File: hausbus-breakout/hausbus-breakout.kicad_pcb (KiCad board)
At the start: 2 copper layers, 29.2 x 32.5 mm, 17 parts, among them IC1 ATMEGA328P-M, P1 CONN_01X10, P2 CONN_01X10, P3 CONN_01X02, P4 CONN_01X02, U1 MCP2515-I/ST, U2 PCA82C251, Y1 16MHz

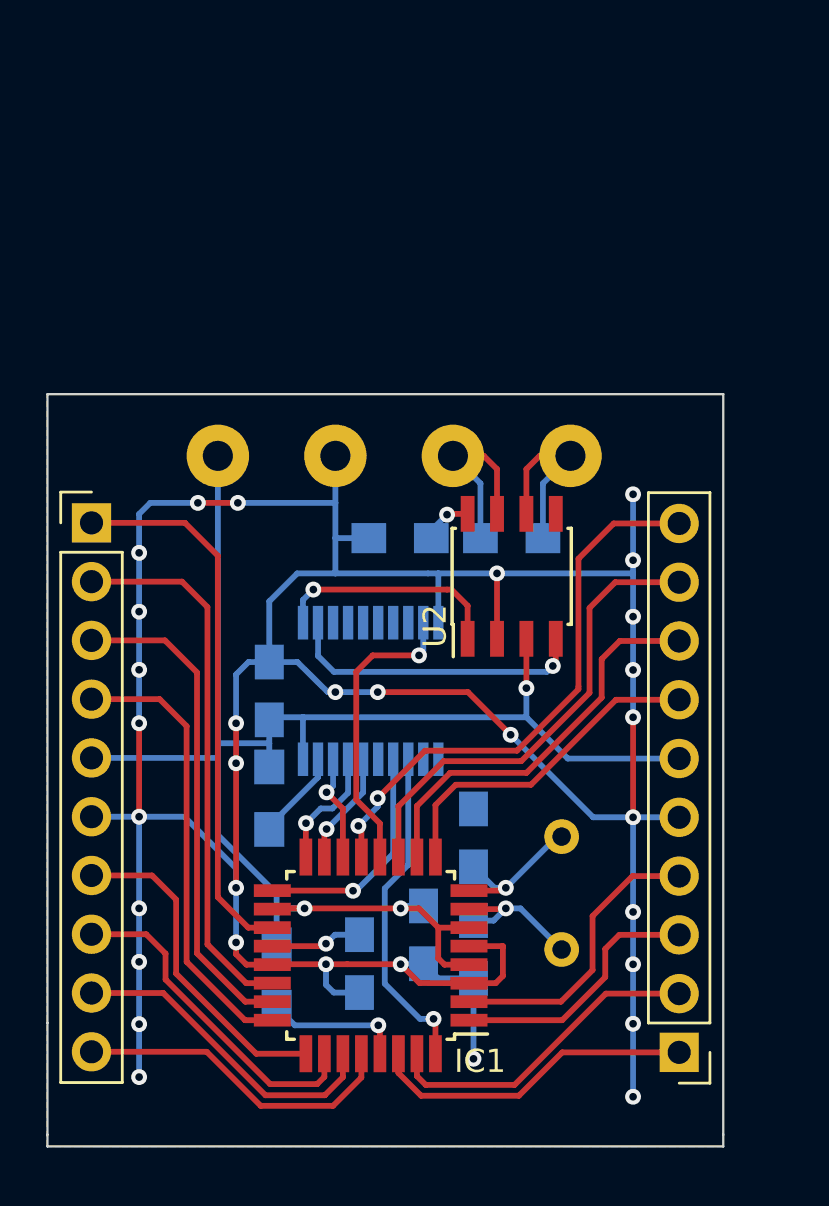
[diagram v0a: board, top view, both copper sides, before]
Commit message: updated breakout to have all four hardware pwm pins of timer 0 and 1 available
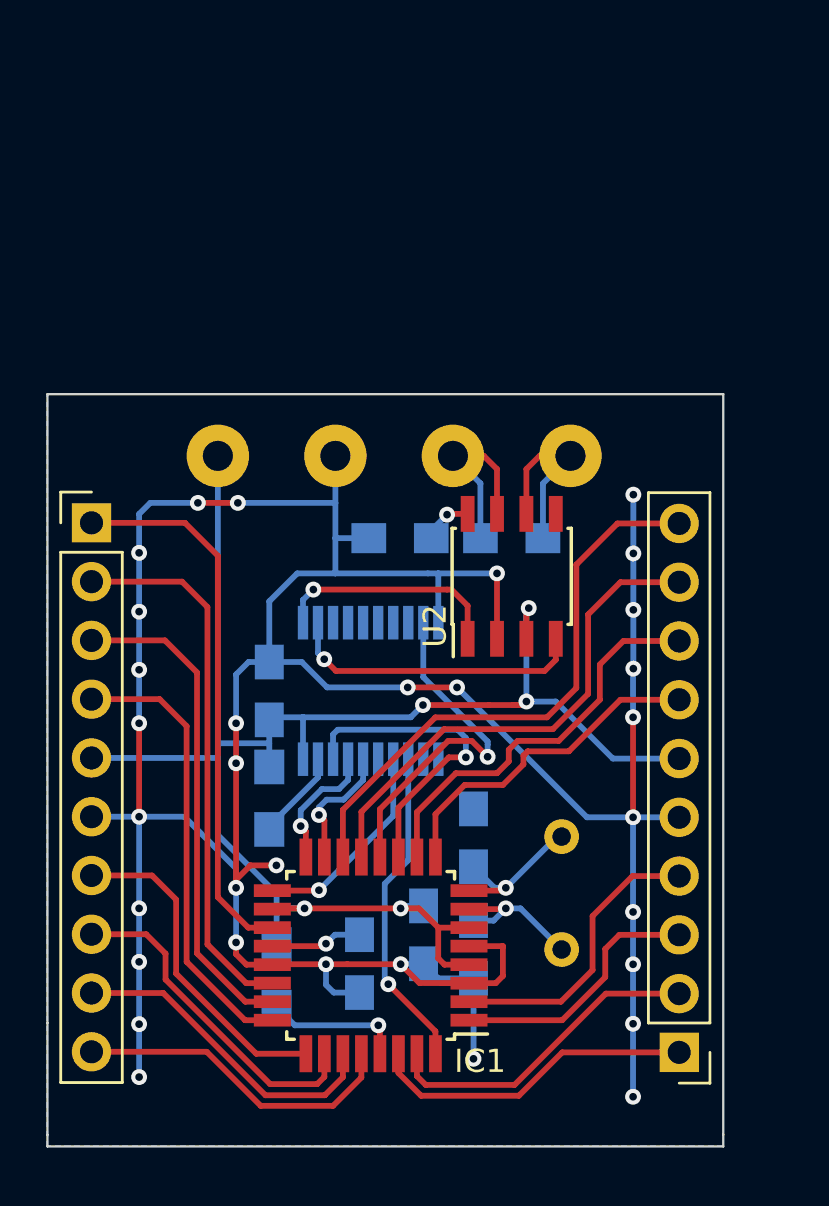
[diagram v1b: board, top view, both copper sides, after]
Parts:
- R1: value term. opt. -> 120R
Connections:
- IC1 pad 11: Net-(IC1-Pad11) -> SS
- IC1 pad 14: SS -> Net-(IC1-Pad14)
- P1 pad 10: Net-(IC1-Pad13) -> Net-(IC1-Pad14)
- P1 pad 9: Net-(IC1-Pad11) -> Net-(IC1-Pad13)
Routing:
- net Net-(IC1-Pad14): track 0.00 -> 24.8 mm
- net Net-(IC1-Pad11): track 20.5 -> 0.00 mm
- net SS: track 4.64 -> 13.8 mm
- net GND: track 156.0 -> 152.5 mm
- net +5V: track 69.8 -> 72.4 mm, vias 3 -> 5
- net Net-(IC1-Pad13): track 24.2 -> 21.8 mm, vias 2 -> 0
- net CLKO: track 12.9 -> 15.2 mm
- net SCK: track 9.97 -> 9.01 mm
- net MOSI: track 4.92 -> 5.55 mm
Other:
- board text added: "B2 B1 D6 D5 5V GND D4 D3 D1 D0"
- board text removed: "B1 D7 D6 D5 5V GND D4 D3 D1 D0"

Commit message: added usb2serial converter header
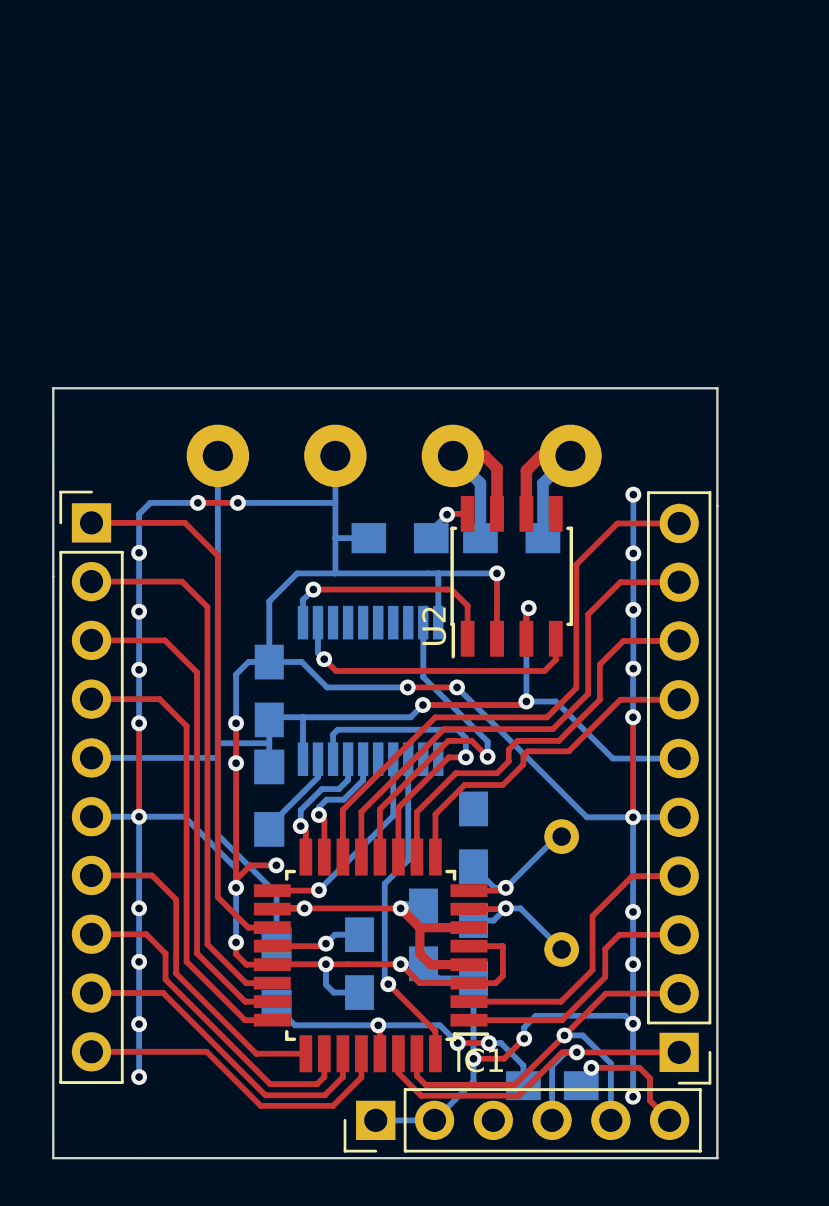
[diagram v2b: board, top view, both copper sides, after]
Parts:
- added C6: 100n, Capacitors_SMD:C_0805_HandSoldering, B.Cu at (215.6, 123.9)
- added P5: CONN_01X06, Socket_Strips:Socket_Strip_Straight_1x06_Pitch2.54mm, F.Cu at (208.0, 125.4)
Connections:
- net Net-(IC1-Pad29) renamed RS
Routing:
- net GND: track 152.5 -> 166.5 mm, vias 32 -> 33
- net RS: track 6.07 -> 13.9 mm, vias 1 -> 3
- net Net-(C6-Pad1): track 0.00 -> 5.85 mm, vias 0 -> 1
- net Net-(IC1-Pad31): track 14.1 -> 19.1 mm, vias 0 -> 1
- net Net-(IC1-Pad30): track 14.2 -> 17.8 mm, vias 0 -> 1
- net +5V: track 72.4 -> 73.1 mm
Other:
- board size 29.2 x 32.5 mm -> 28.7 x 33.3 mm
- net class buslines added: clearance 0.2, trace_width 0.5, via_dia 0.6858, via_drill 0.3302
- net class power added: clearance 0.2, trace_width 0.4, via_dia 0.6858, via_drill 0.3302
- board text added: "*B2 *B1 *D6 *D5 5V GND D4 D3 D1 D0"
- board text added: "ADC6 ADC7 C0 C1 5V GND C2 C3 C4 C5"
- board text removed: "B2 B1 D6 D5 5V GND D4 D3 D1 D0"
- board text removed: "C6 C7 C0 C1 5V GND C2 C3 C4 C5"

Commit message: cleanup of schematic, added rj45 jacks for can bus
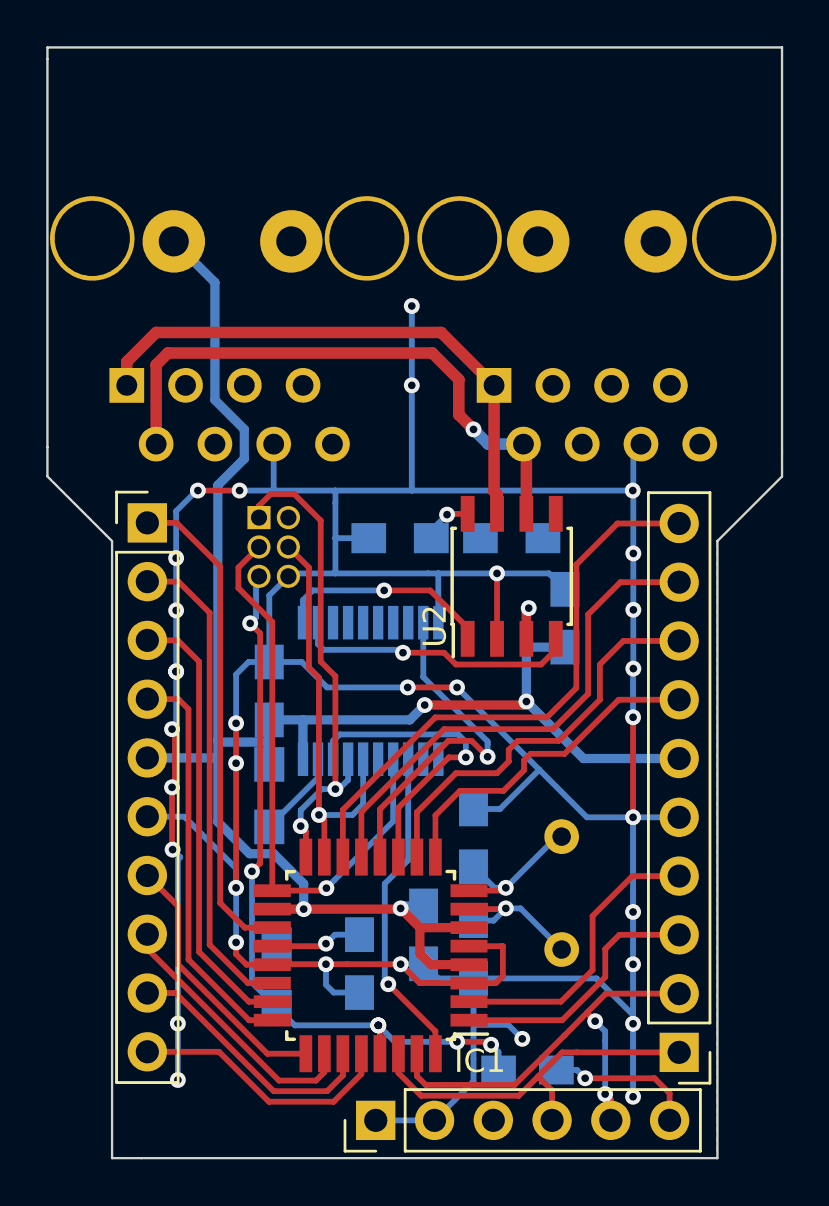
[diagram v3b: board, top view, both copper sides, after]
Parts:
- added C7: 100nF, Capacitors_SMD:C_0805_HandSoldering, B.Cu at (216.2, 103.7)
- added CON1: AVR-ISP-6, Socket_Strips:Socket_Strip_Straight_2x03_Pitch1.27mm, B.Cu at (202.9, 99.3)
- added J1: RJ45, Connect:RJ45_8, B.Cu at (197.2, 93.6)
- added J2: RJ45, Connect:RJ45_8, B.Cu at (213.1, 93.6)
- moved P3 9.98 mm to (215.0, 87.4)
- moved P4 9.46 mm to (199.3, 87.4)
- moved P2 2.41 mm to (198.1, 99.5)
- moved C6 1.27 mm to (214.5, 123.2)
- moved R3 0.11 mm to (203.4, 111.3)
- turned R2 to 270 degrees
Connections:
- net Net-(IC1-Pad1) renamed D3
- net Net-(IC1-Pad10) renamed D6
- net Net-(IC1-Pad13) renamed B1
- net Net-(IC1-Pad14) renamed B2
- net Net-(IC1-Pad19) renamed ADC6
- net Net-(IC1-Pad2) renamed D4
- net Net-(IC1-Pad22) renamed ADC7
- net Net-(IC1-Pad23) renamed C0
- net Net-(IC1-Pad24) renamed C1
- net Net-(IC1-Pad25) renamed C2
- net Net-(IC1-Pad26) renamed C3
- net Net-(IC1-Pad27) renamed C4
- net Net-(IC1-Pad28) renamed C5
- net Net-(IC1-Pad30) renamed D0
- net Net-(IC1-Pad31) renamed D1
- net Net-(IC1-Pad9) renamed D5
- R2 pad 1: RS -> +5V
- R2 pad 2: +5V -> RS
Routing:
- net GND: track 166.5 -> 193.7 mm
- net CANLOW: track 8.09 -> 26.6 mm, vias 0 -> 1
- net RS: track 13.9 -> 32.1 mm, vias 3 -> 6
- net SCK: track 9.01 -> 25.9 mm
- net MISO: track 5.60 -> 21.5 mm, vias 1 -> 2
- net CANHIGH: track 8.66 -> 24.0 mm
- net MOSI: track 5.55 -> 18.1 mm
- net +5V: track 73.1 -> 82.6 mm
- net C3: track 14.5 -> 11.6 mm
- net C2: track 14.3 -> 11.5 mm
- net C5: track 14.2 -> 11.5 mm
- net C4: track 14.0 -> 11.4 mm
- net ADC7: track 23.5 -> 21.0 mm
- net ADC6: track 23.7 -> 21.2 mm
- net C0: track 21.4 -> 19.2 mm
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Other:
- board size 28.7 x 33.3 mm -> 31.8 x 48 mm

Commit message: many changes have been done to the breakout
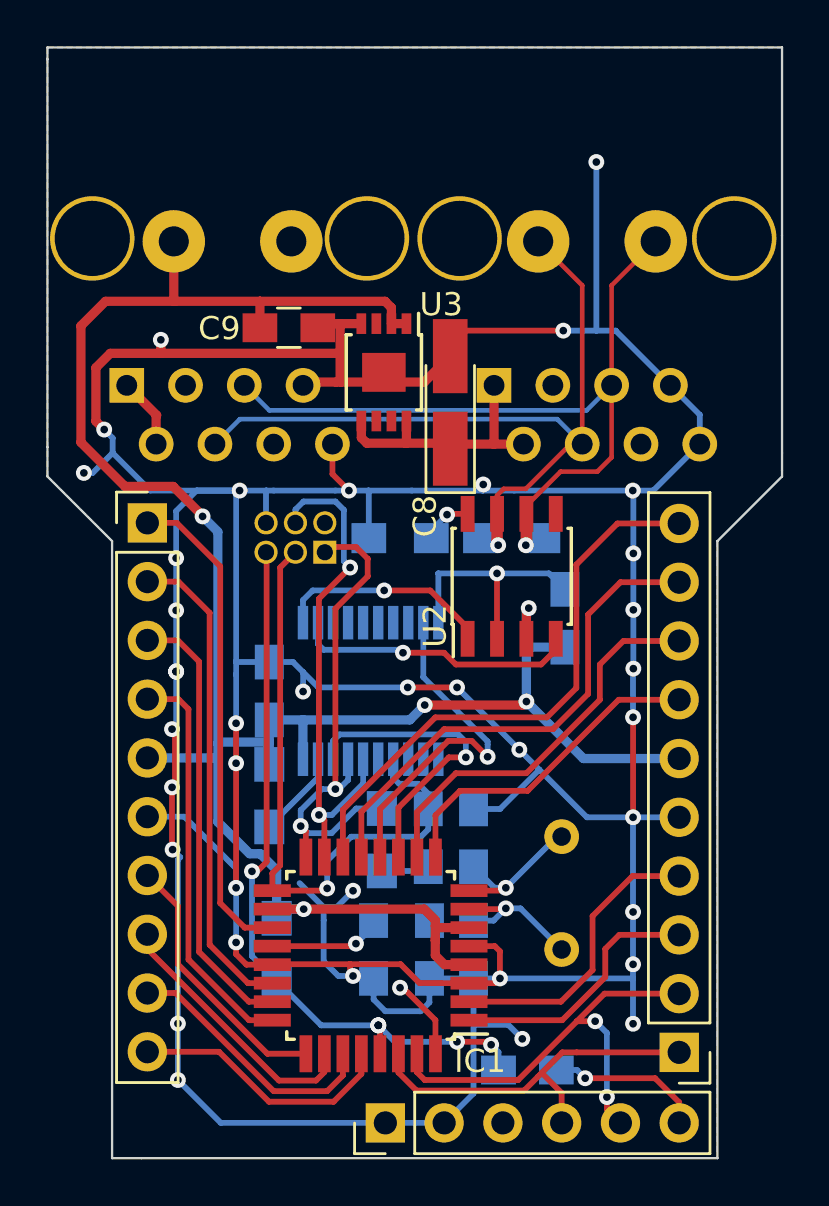
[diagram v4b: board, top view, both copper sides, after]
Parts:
- added C10: 10n, Capacitors_SMD:C_0805_HandSoldering, B.Cu at (210.3, 113.2)
- added C8: 1u, Capacitors_Tantalum_SMD:CP_Tantalum_Case-A_EIA-3216-18_Hand, F.Cu at (211.2, 94.3)
- added C9: 1u, Capacitors_SMD:C_0805_HandSoldering, F.Cu at (204.2, 91.1)
- added R5: 1k, Resistors_SMD:R_0805_HandSoldering, B.Cu at (208.3, 113.2)
- added U3: LT3010-5, Housings_SSOP:MSOP-8-1EP_3x3mm_Pitch0.65mm, F.Cu at (208.3, 93.0)
- CON1: moved to F.Cu
- moved CON1 3.22 mm to (205.8, 100.8), turned to 270 degrees
- moved R2 1.14 mm to (203.7, 118.0)
- moved C5 0.86 mm to (207.9, 118.0)
- moved C2 0.68 mm to (210.3, 118.0)
- moved P5 0.43 mm to (208.4, 125.5)
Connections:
- J1 pad 1: CANHIGH -> VCOM
- J1 pad 2: CANLOW -> VCOM
- J1 pad 3: GND -> (no net)
- J1 pad 4: (no net) -> CAN+
- J1 pad 5: (no net) -> CAN-
- J1 pad 6: GND -> (no net)
- J1 pad 7: (no net) -> GND
- J1 pad 8: (no net) -> GND
- J2 pad 1: CANHIGH -> VCOM
- J2 pad 2: CANLOW -> VCOM
- J2 pad 3: GND -> (no net)
- J2 pad 4: (no net) -> CAN+
- J2 pad 5: (no net) -> CAN-
- J2 pad 6: GND -> (no net)
- J2 pad 7: (no net) -> GND
- J2 pad 8: (no net) -> GND
- P3 pad 1: CANHIGH -> CAN+
- P3 pad 2: CANLOW -> CAN-
- R1 pad 1: CANLOW -> CAN-
- R1 pad 2: CANHIGH -> CAN+
- U2 pad 6: CANLOW -> CAN-
- U2 pad 7: CANHIGH -> CAN+
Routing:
- net GND: track 193.7 -> 259.1 mm, vias 33 -> 39
- net CAN-: track 0.00 -> 34.2 mm, vias 0 -> 1
- net CAN+: track 0.00 -> 34.0 mm, vias 0 -> 1
- net CANLOW: track 26.6 -> 0.00 mm, vias 1 -> 0
- net CANHIGH: track 24.0 -> 0.00 mm
- net +5V: track 82.6 -> 99.0 mm
- net VCOM: track 0.00 -> 15.2 mm
- net INT0: track 14.1 -> 3.56 mm
- net MOSI: track 18.1 -> 22.3 mm, vias 1 -> 2
- net Net-(C10-Pad2): track 0.00 -> 2.45 mm
- net SCK: track 25.9 -> 28.2 mm
- net MISO: track 21.5 -> 22.5 mm
- net Net-(C5-Pad1): track 3.97 -> 4.97 mm
- net RS: track 32.1 -> 32.4 mm, vias 6 -> 5
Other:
- net class buslines: clearance 0.2 -> 0.15; trace_width 0.5 -> 0.2
- board text added: "all pins marked with * are capable of pwm"
